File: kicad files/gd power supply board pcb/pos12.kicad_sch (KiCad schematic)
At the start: 31 parts

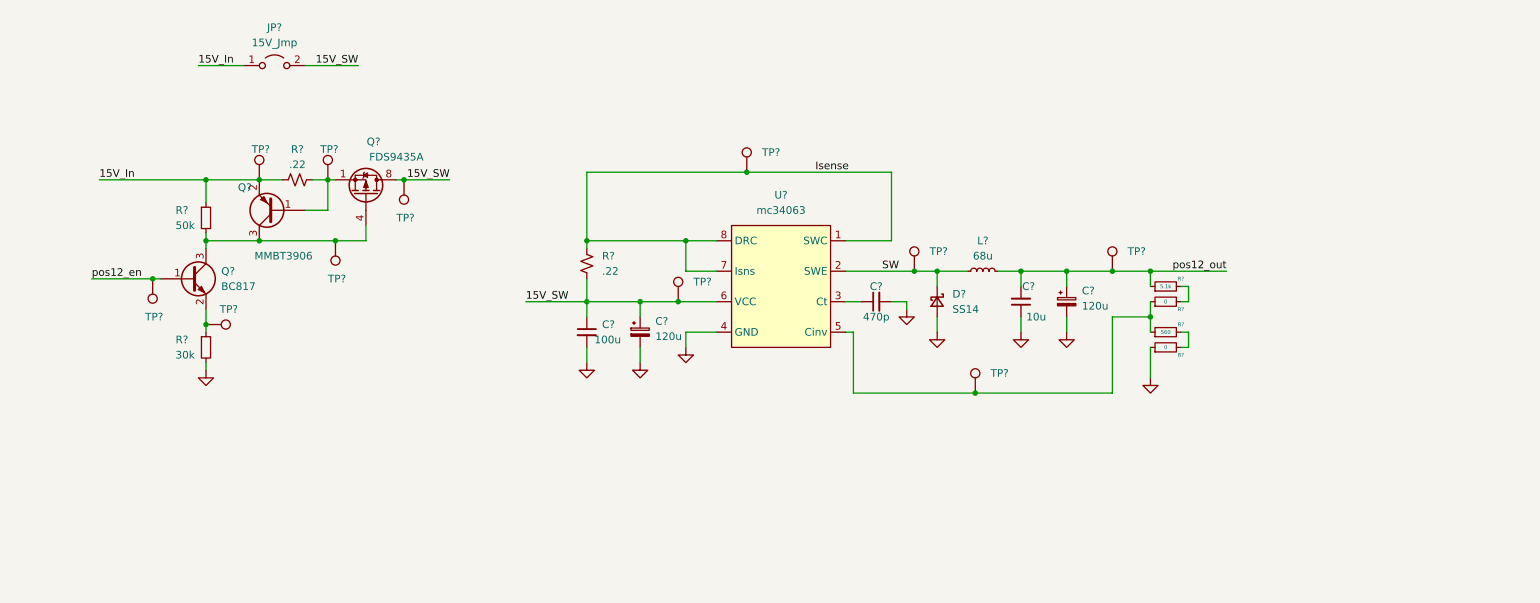
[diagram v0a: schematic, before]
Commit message: cleaned up labels and footprints
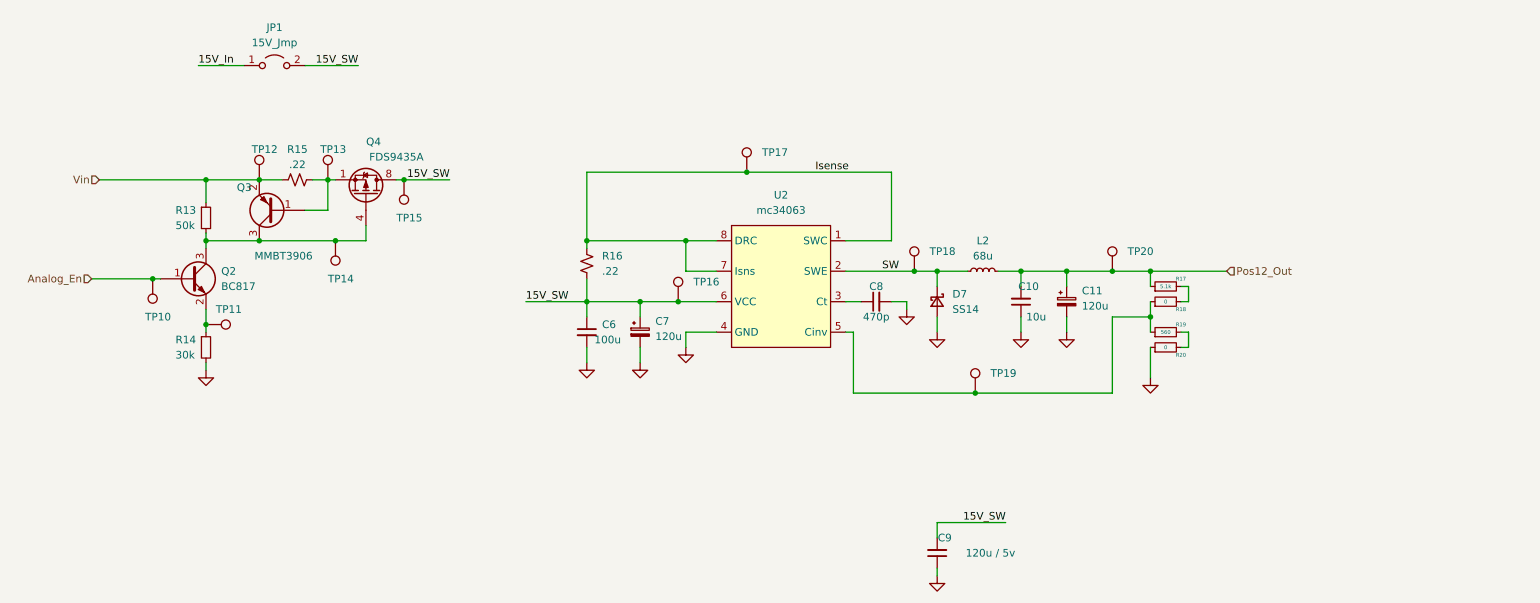
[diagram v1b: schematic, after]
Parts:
- added C9: 120u / 5v, Capacitor_SMD:C_0805_2012Metric, symbol My Library:C_0805
- R13, R14: renamed from R?; footprint (none) -> Resistor_SMD:R_0805_2012Metric
- U2: renamed from U?; footprint (none) -> Package_SO:SOIC-8_3.9x4.9mm_P1.27mm
- gave numbers to parts that had none: 28
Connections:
- net 15V_In: no longer Q3.2 (E), R13.1, R15.1, TP12.1
- net 15V_SW: now also C9.2
- net GND: now also C9.1
- net pos12_en renamed Analog_En
- net pos12_out renamed Pos12_Out
- new net Vin: Q3.2 (E), R13.1, R15.1, TP12.1

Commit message: before erc
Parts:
- added H5, H6, H7, H8: MountingHole, MountingHole:MountingHole_2.2mm_M2, symbol Mechanical:MountingHole
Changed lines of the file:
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@@
     (pin "2")
+  )
+  (symbol (lib_id "Mechanical:MountingHole") (at 179.07 60.96 0) (unit 1)
+    (in_bom yes) (on_board yes) (fields_autoplaced)
+    (property "Reference" "H6" (id 0) (at 181.61 59.6899 0)
+      (effects (font (size 1.27 1.27)) (justify left))
+    )
+    (property "Value" "MountingHole" (id 1) (at 181.61 62.2299 0)
+      (effects (font (size 1.27 1.27)) (justify left))
+    )
+    (property "Footprint" "MountingHole:MountingHole_2.2mm_M2" (id 2) (at 179.07 60.96 0)
+      (effects (font (size 1.27 1.27)) hide)
+    )
+    (property "Datasheet" "~" (id 3) (at 179.07 60.96 0)
+      (effects (font (size 1.27 1.27)) hide)
+    )
   )
   (symbol (lib_id "My Library:TestPoint_Harwin") (at 45.72 96.52 180) (unit 1)
@@
     (pin "1")
   )
+  (symbol (lib_id "Mechanical:MountingHole") (at 187.96 54.61 0) (unit 1)
+    (in_bom yes) (on_board yes) (fields_autoplaced)
+    (property "Reference" "H7" (id 0) (at 190.5 53.3399 0)
+      (effects (font (size 1.27 1.27)) (justify left))
+    )
+    (property "Value" "MountingHole" (id 1) (at 190.5 55.8799 0)
+      (effects (font (size 1.27 1.27)) (justify left))
+    )
+    (property "Footprint" "MountingHole:MountingHole_2.2mm_M2" (id 2) (at 187.96 54.61 0)
+      (effects (font (size 1.27 1.27)) hide)
+    )
+    (property "Datasheet" "~" (id 3) (at 187.96 54.61 0)
+      (effects (font (size 1.27 1.27)) hide)
+    )
+  )
   (symbol (lib_id "My Library:TestPoint_Harwin") (at 87.63 80.01 180) (unit 1)
     (in_bom yes) (on_board yes)
@@
     )
     (pin "1")
+  )
+  (symbol (lib_id "Mechanical:MountingHole") (at 179.07 54.61 0) (unit 1)
+    (in_bom yes) (on_board yes) (fields_autoplaced)
+    (property "Reference" "H5" (id 0) (at 181.61 53.3399 0)
+      (effects (font (size 1.27 1.27)) (justify left))
+    )
+    (property "Value" "MountingHole" (id 1) (at 181.61 55.8799 0)
+      (effects (font (size 1.27 1.27)) (justify left))
+    )
+    (property "Footprint" "MountingHole:MountingHole_2.2mm_M2" (id 2) (at 179.07 54.61 0)
+      (effects (font (size 1.27 1.27)) hide)
+    )
+    (property "Datasheet" "~" (id 3) (at 179.07 54.61 0)
+      (effects (font (size 1.27 1.27)) hide)
+    )
   )
   (symbol (lib_id "power:GND") (at 198.12 105.41 0) (unit 1)
@@
     (pin "1")
   )
+  (symbol (lib_id "Mechanical:MountingHole") (at 187.96 60.96 0) (unit 1)
+    (in_bom yes) (on_board yes) (fields_autoplaced)
+    (property "Reference" "H8" (id 0) (at 190.5 59.6899 0)
+      (effects (font (size 1.27 1.27)) (justify left))
+    )
+    (property "Value" "MountingHole" (id 1) (at 190.5 62.2299 0)
+      (effects (font (size 1.27 1.27)) (justify left))
+    )
+    (property "Footprint" "MountingHole:MountingHole_2.2mm_M2" (id 2) (at 187.96 60.96 0)
+      (effects (font (size 1.27 1.27)) hide)
+    )
+    (property "Datasheet" "~" (id 3) (at 187.96 60.96 0)
+      (effects (font (size 1.27 1.27)) hide)
+    )
+  )
   (symbol (lib_id "Jumper:Jumper_2_Open") (at 66.04 60.96 0) (unit 1)

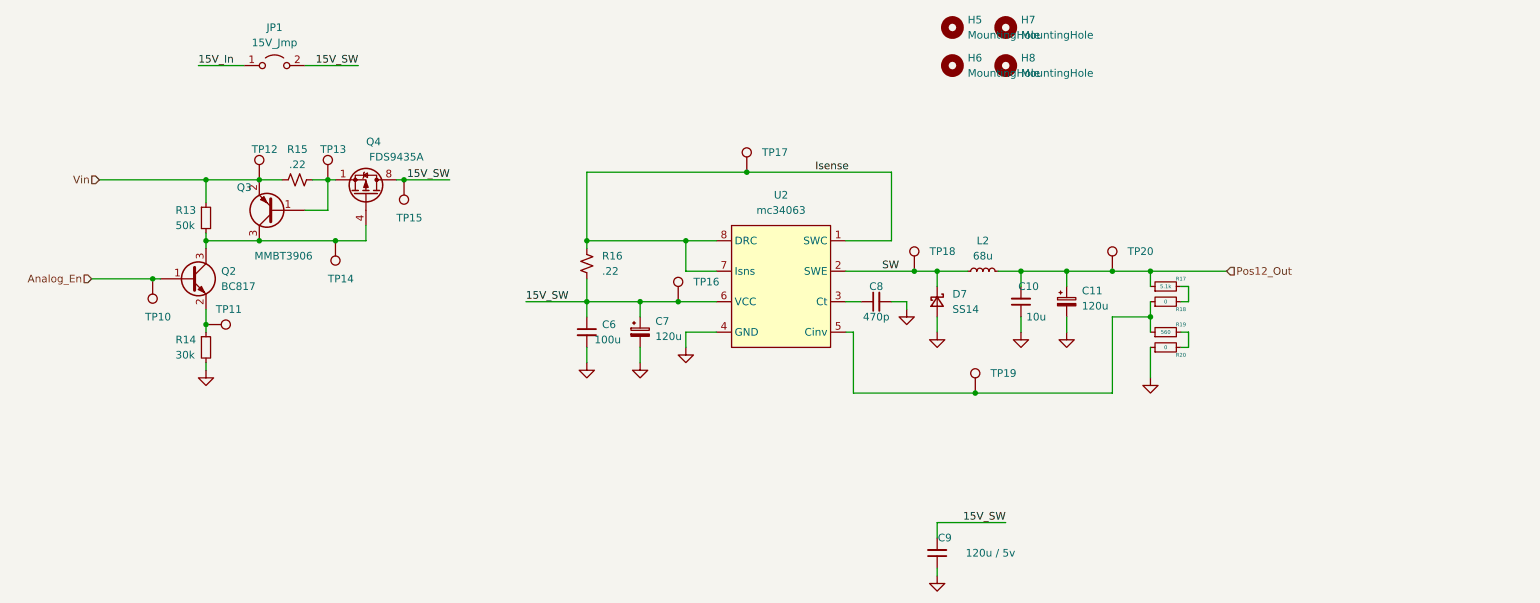
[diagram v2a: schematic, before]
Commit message: initial floor planning done
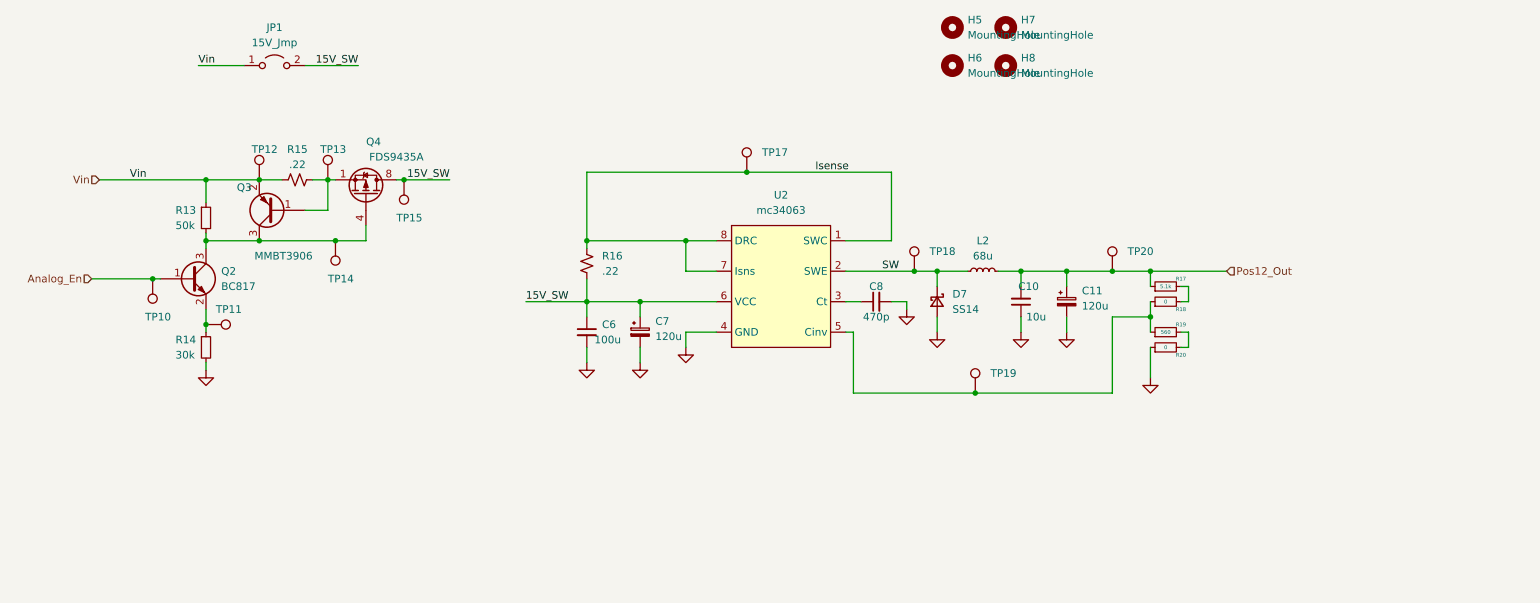
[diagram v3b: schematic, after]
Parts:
- removed C9: 120u / 5v, Capacitor_SMD:C_0805_2012Metric, symbol My Library:C_0805
- removed TP16: TestPoint_Harwin, My Libraries:Harwin-S1751-46-Test-Point, symbol My Library:TestPoint_Harwin
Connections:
- net 15V_In is gone; now on net Vin: JP1.1 (A)
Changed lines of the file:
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@@
   (junction (at 118.11 100.33) (diameter 0) (color 0 0 0 0)
   )
-  (junction (at 133.35 100.33) (diameter 0) (color 0 0 0 0)
-  )
   (junction (at 118.11 90.17) (diameter 0) (color 0 0 0 0)
   )
@@
     (stroke (width 0) (type default) (color 0 0 0 0))
   )
-  (wire (pts (xy 127 100.33) (xy 133.35 100.33))
-    (stroke (width 0) (type default) (color 0 0 0 0))
-  )
   (wire (pts (xy 172.72 95.25) (xy 176.53 95.25))
     (stroke (width 0) (type default) (color 0 0 0 0))
@@
     (stroke (width 0) (type default) (color 0 0 0 0))
   )
-  (wire (pts (xy 133.35 100.33) (xy 139.7 100.33))
+  (wire (pts (xy 127 100.33) (xy 139.7 100.33))
     (stroke (width 0) (type default) (color 0 0 0 0))
   )
@@
     (stroke (width 0) (type default) (color 0 0 0 0))
   )
-  (wire (pts (xy 176.53 137.16) (xy 176.53 139.7))
-    (stroke (width 0) (type default) (color 0 0 0 0))
-  )
   (wire (pts (xy 74.93 80.01) (xy 76.2 80.01))
     (stroke (width 0) (type default) (color 0 0 0 0))
@@
     (stroke (width 0) (type default) (color 0 0 0 0))
   )
-  (wire (pts (xy 176.53 144.78) (xy 176.53 146.05))
-    (stroke (width 0) (type default) (color 0 0 0 0))
-  )
   (wire (pts (xy 212.09 102.87) (xy 212.09 105.41))
     (stroke (width 0) (type default) (color 0 0 0 0))
@@
   )
   (wire (pts (xy 35.56 96.52) (xy 45.72 96.52))
-    (stroke (width 0) (type default) (color 0 0 0 0))
-  )
-  (wire (pts (xy 176.53 137.16) (xy 187.96 137.16))
     (stroke (width 0) (type default) (color 0 0 0 0))
   )
@@
     (effects (font (size 1.27 1.27)) (justify left bottom))
   )
-  (label "15V_SW" (at 187.96 137.16 180)
-    (effects (font (size 1.27 1.27)) (justify right bottom))
+  (label "Vin" (at 41.91 80.01 0)
+    (effects (font (size 1.27 1.27)) (justify left bottom))
   )
   (label "15V_SW" (at 107.95 100.33 0)
     (effects (font (size 1.27 1.27)) (justify left bottom))
   )
-  (label "15V_In" (at 53.34 60.96 0)
+  (label "Vin" (at 53.34 60.96 0)
     (effects (font (size 1.27 1.27)) (justify left bottom))
   )
@@
     (pin "1")
     (pin "2")
-  )
-  (symbol (lib_id "power:GND") (at 176.53 146.05 0) (unit 1)
-    (in_bom yes) (on_board yes) (fields_autoplaced)
-    (property "Reference" "#PWR0119" (id 0) (at 176.53 152.4 0)
-      (effects (font (size 1.27 1.27)) hide)
-    )
-    (property "Value" "GND" (id 1) (at 176.53 151.13 0)
-      (effects (font (size 1.27 1.27)) hide)
-    )
-    (property "Footprint" "" (id 2) (at 176.53 146.05 0)
-      (effects (font (size 1.27 1.27)) hide)
-    )
-    (property "Datasheet" "" (id 3) (at 176.53 146.05 0)
-      (effects (font (size 1.27 1.27)) hide)
-    )
-    (pin "1")
-  )
-  (symbol (lib_id "My Library:TestPoint_Harwin") (at 133.35 100.33 0) (unit 1)
-    (in_bom yes) (on_board yes) (fields_autoplaced)
-    (property "Reference" "TP16" (id 0) (at 135.89 97.0279 0)
-      (effects (font (size 1.27 1.27)) (justify left))
-    )
-    (property "Value" "TestPoint_Harwin" (id 1) (at 133.35 95.25 0)
-      (effects (font (size 1.27 1.27)) hide)
-    )
-    (property "Footprint" "My Libraries:Harwin-S1751-46-Test-Point" (id 2) (at 138.43 100.33 0)
-      (effects (font (size 1.27 1.27)) hide)
-    )
-    (property "Datasheet" "~" (id 3) (at 138.43 100.33 0)
-      (effects (font (size 1.27 1.27)) hide)
-    )
-    (pin "1")
   )
   (symbol (lib_id "My Library:TestPoint_Harwin") (at 74.93 80.01 0) (unit 1)
@@
       (effects (font (size 1.27 1.27)) hide)
     )
-    (pin "1")
-    (pin "2")
-  )
-  (symbol (lib_id "My Library:C_0805") (at 176.53 142.24 180) (unit 1)
-    (in_bom yes) (on_board yes)
-    (property "Reference" "C9" (id 0) (at 177.8 139.7 0))
-    (property "Value" "120u / 5v" (id 1) (at 185.42 142.24 0))
-    (property "Footprint" "Capacitor_SMD:C_0805_2012Metric" (id 2) (at 176.53 142.24 0)
-      (effects (font (size 1.27 1.27)) hide)
-    )
-    (property "Datasheet" "~" (id 3) (at 176.53 142.24 0)
-      (effects (font (size 1.27 1.27)) hide)
-    )

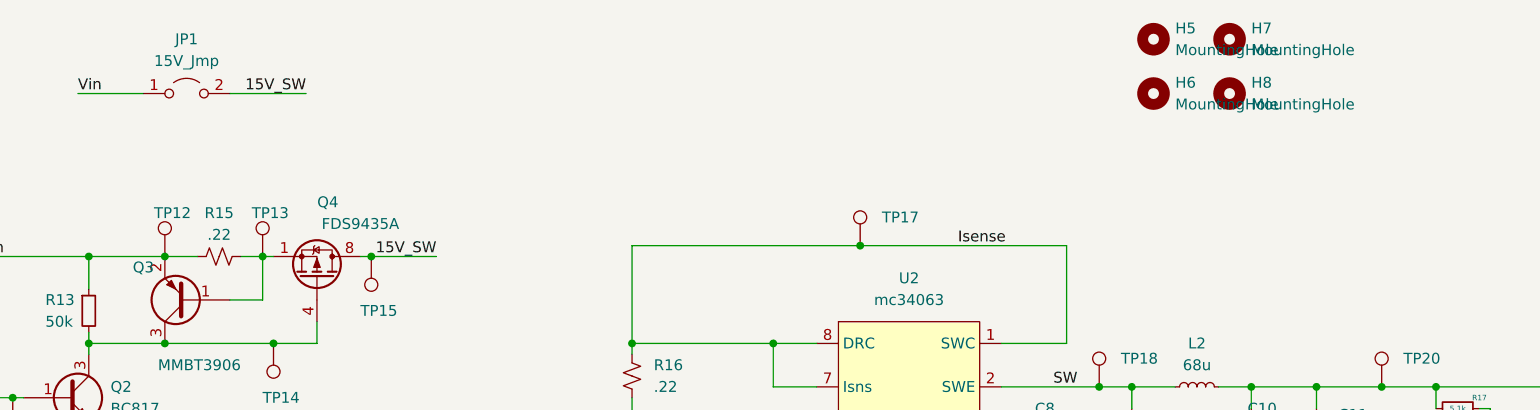
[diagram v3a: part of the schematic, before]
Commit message: minor fixes and compacting the floorplan. stacked 5V supplies for maximum minimage.
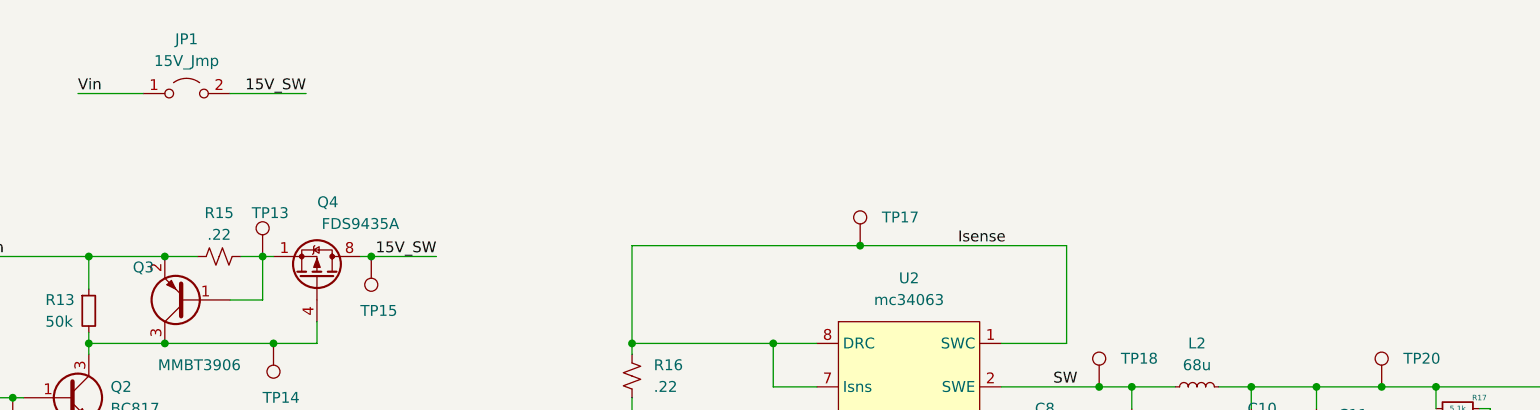
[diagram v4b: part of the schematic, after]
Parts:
- removed H5, H6, H7, H8: MountingHole, MountingHole:MountingHole_2.2mm_M2, symbol Mechanical:MountingHole
- removed TP12: TestPoint_Harwin, My Libraries:Harwin-S1751-46-Test-Point, symbol My Library:TestPoint_Harwin
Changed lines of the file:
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@@
     (effects (font (size 1.27 1.27)) (justify right))
-  )
-  (symbol (lib_id "My Library:TestPoint_Harwin") (at 63.5 80.01 0) (unit 1)
-    (in_bom yes) (on_board yes)
-    (property "Reference" "TP12" (id 0) (at 62.23 74.93 0)
-      (effects (font (size 1.27 1.27)) (justify left))
-    )
-    (property "Value" "TestPoint_Harwin" (id 1) (at 63.5 74.93 0)
-      (effects (font (size 1.27 1.27)) hide)
-    )
-    (property "Footprint" "My Libraries:Harwin-S1751-46-Test-Point" (id 2) (at 68.58 80.01 0)
-      (effects (font (size 1.27 1.27)) hide)
-    )
-    (property "Datasheet" "~" (id 3) (at 68.58 80.01 0)
-      (effects (font (size 1.27 1.27)) hide)
-    )
-    (pin "1")
   )
   (symbol (lib_id "My Library:TestPoint_Harwin") (at 54.61 104.14 270) (unit 1)
@@
     (pin "2")
   )
-  (symbol (lib_id "Mechanical:MountingHole") (at 179.07 60.96 0) (unit 1)
-    (in_bom yes) (on_board yes) (fields_autoplaced)
-    (property "Reference" "H6" (id 0) (at 181.61 59.6899 0)
-      (effects (font (size 1.27 1.27)) (justify left))
-    )
-    (property "Value" "MountingHole" (id 1) (at 181.61 62.2299 0)
-      (effects (font (size 1.27 1.27)) (justify left))
-    )
-    (property "Footprint" "MountingHole:MountingHole_2.2mm_M2" (id 2) (at 179.07 60.96 0)
-      (effects (font (size 1.27 1.27)) hide)
-    )
-    (property "Datasheet" "~" (id 3) (at 179.07 60.96 0)
-      (effects (font (size 1.27 1.27)) hide)
-    )
-  )
   (symbol (lib_id "My Library:TestPoint_Harwin") (at 45.72 96.52 180) (unit 1)
     (in_bom yes) (on_board yes)
@@
     (pin "1")
   )
-  (symbol (lib_id "Mechanical:MountingHole") (at 187.96 54.61 0) (unit 1)
-    (in_bom yes) (on_board yes) (fields_autoplaced)
-    (property "Reference" "H7" (id 0) (at 190.5 53.3399 0)
-      (effects (font (size 1.27 1.27)) (justify left))
-    )
-    (property "Value" "MountingHole" (id 1) (at 190.5 55.8799 0)
-      (effects (font (size 1.27 1.27)) (justify left))
-    )
-    (property "Footprint" "MountingHole:MountingHole_2.2mm_M2" (id 2) (at 187.96 54.61 0)
-      (effects (font (size 1.27 1.27)) hide)
-    )
-    (property "Datasheet" "~" (id 3) (at 187.96 54.61 0)
-      (effects (font (size 1.27 1.27)) hide)
-    )
-  )
   (symbol (lib_id "My Library:TestPoint_Harwin") (at 87.63 80.01 180) (unit 1)
     (in_bom yes) (on_board yes)
@@
     )
     (pin "1")
-  )
-  (symbol (lib_id "Mechanical:MountingHole") (at 179.07 54.61 0) (unit 1)
-    (in_bom yes) (on_board yes) (fields_autoplaced)
-    (property "Reference" "H5" (id 0) (at 181.61 53.3399 0)
-      (effects (font (size 1.27 1.27)) (justify left))
-    )
-    (property "Value" "MountingHole" (id 1) (at 181.61 55.8799 0)
-      (effects (font (size 1.27 1.27)) (justify left))
-    )
-    (property "Footprint" "MountingHole:MountingHole_2.2mm_M2" (id 2) (at 179.07 54.61 0)
-      (effects (font (size 1.27 1.27)) hide)
-    )
-    (property "Datasheet" "~" (id 3) (at 179.07 54.61 0)
-      (effects (font (size 1.27 1.27)) hide)
-    )
   )
   (symbol (lib_id "power:GND") (at 198.12 105.41 0) (unit 1)
@@
     (pin "1")
   )
-  (symbol (lib_id "Mechanical:MountingHole") (at 187.96 60.96 0) (unit 1)
-    (in_bom yes) (on_board yes) (fields_autoplaced)
-    (property "Reference" "H8" (id 0) (at 190.5 59.6899 0)
-      (effects (font (size 1.27 1.27)) (justify left))
-    )
-    (property "Value" "MountingHole" (id 1) (at 190.5 62.2299 0)
-      (effects (font (size 1.27 1.27)) (justify left))
-    )
-    (property "Footprint" "MountingHole:MountingHole_2.2mm_M2" (id 2) (at 187.96 60.96 0)
-      (effects (font (size 1.27 1.27)) hide)
-    )
-    (property "Datasheet" "~" (id 3) (at 187.96 60.96 0)
-      (effects (font (size 1.27 1.27)) hide)
-    )
-  )
   (symbol (lib_id "Jumper:Jumper_2_Open") (at 66.04 60.96 0) (unit 1)

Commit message: pre-routing try 1
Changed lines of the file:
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@@
     (effects (font (size 1.27 1.27)) (justify left bottom))
+  )
+  (label "Pos12_Out" (at 219.71 95.25 180)
+    (effects (font (size 1.27 1.27)) (justify right bottom))
   )
   (label "15V_SW" (at 80.01 60.96 180)
